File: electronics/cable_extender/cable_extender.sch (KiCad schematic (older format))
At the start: 2 parts

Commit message: added initial connections for the 2.54mm grid (possibly
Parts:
- added J? (x2): Conn_01x08, symbol Connector_Generic:Conn_01x08
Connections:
- net labels added: PIN_01, PIN_02, PIN_03, PIN_04, PIN_05, PIN_06, PIN_07, PIN_08
- wire segments 0 -> 8
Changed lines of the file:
@@
 Wire Notes Line
 	600  7550 1400 7550
+$Comp
+L Connector_Generic:Conn_01x08 J?
+U 1 1 5EE7D502
+P 950 1450
+F 0 "J?" H 868 825 50  0000 C CNN
+F 1 "Conn_01x08" H 868 916 50  0000 C CNN
+F 2 "" H 950 1450 50  0001 C CNN
+F 3 "~" H 950 1450 50  0001 C CNN
+	1    950  1450
+	-1   0    0    1
+$EndComp
+Text Label 1200 1750 0    50   ~ 0
+PIN_01
+Text Label 1200 1650 0    50   ~ 0
+PIN_02
+Text Label 1200 1550 0    50   ~ 0
+PIN_03
+Text Label 1200 1450 0    50   ~ 0
+PIN_04
+Text Label 1200 1350 0    50   ~ 0
+PIN_05
+Text Label 1200 1250 0    50   ~ 0
+PIN_06
+Text Label 1200 1150 0    50   ~ 0
+PIN_07
+Text Label 1200 1050 0    50   ~ 0
+PIN_08
+$Comp
+L Connector_Generic:Conn_01x08 J?
+U 1 1 5EE7E83D
+P 1700 1450
+F 0 "J?" H 1618 825 50  0000 C CNN
+F 1 "Conn_01x08" H 1618 916 50  0000 C CNN
+F 2 "" H 1700 1450 50  0001 C CNN
+F 3 "~" H 1700 1450 50  0001 C CNN
+	1    1700 1450
+	1    0    0    1
+$EndComp
+Wire Wire Line
+	1150 1050 1500 1050
+Wire Wire Line
+	1500 1150 1150 1150
+Wire Wire Line
+	1150 1250 1500 1250
+Wire Wire Line
+	1500 1350 1150 1350
+Wire Wire Line
+	1150 1450 1500 1450
+Wire Wire Line
+	1500 1550 1150 1550
+Wire Wire Line
+	1150 1650 1500 1650
+Wire Wire Line
+	1500 1750 1150 1750
 $EndSCHEMATC

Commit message: updated PCB library, added initial connections
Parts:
- removed J? (x2): Conn_01x08, symbol Connector_Generic:Conn_01x08
- added J? (x2): Conn_01x06, symbol Connector_Generic:Conn_01x06
- added J? (x2): Conn_01x11, symbol Connector_Generic:Conn_01x11
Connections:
- net labels added: PIN_09, PIN_10, PIN_11
- wire segments 8 -> 28
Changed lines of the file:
@@
 Wire Notes Line
 	600  7550 1400 7550
+Text Label 1600 1850 0    50   ~ 0
+PIN_04
+Text Label 1600 1750 0    50   ~ 0
+PIN_05
+Text Label 1600 1650 0    50   ~ 0
+PIN_06
+Text Label 1600 1550 0    50   ~ 0
+PIN_07
+Text Label 1600 1450 0    50   ~ 0
+PIN_08
 $Comp
-L Connector_Generic:Conn_01x08 J?
-U 1 1 5EE7D502
-P 950 1450
-F 0 "J?" H 868 825 50  0000 C CNN
-F 1 "Conn_01x08" H 868 916 50  0000 C CNN
-F 2 "" H 950 1450 50  0001 C CNN
-F 3 "~" H 950 1450 50  0001 C CNN
-	1    950  1450
+L Connector_Generic:Conn_01x06 J?
+U 1 1 5EE7FFB1
+P 1350 1650
+F 0 "J?" H 1350 1250 50  0000 C CNN
+F 1 "Conn_01x06" V 1450 1600 50  0000 C CNN
+F 2 "" H 1350 1650 50  0001 C CNN
+F 3 "~" H 1350 1650 50  0001 C CNN
+	1    1350 1650
 	-1   0    0    1
 $EndComp
-Text Label 1200 1750 0    50   ~ 0
-PIN_01
-Text Label 1200 1650 0    50   ~ 0
-PIN_02
-Text Label 1200 1550 0    50   ~ 0
-PIN_03
-Text Label 1200 1450 0    50   ~ 0
-PIN_04
-Text Label 1200 1350 0    50   ~ 0
-PIN_05
-Text Label 1200 1250 0    50   ~ 0
-PIN_06
-Text Label 1200 1150 0    50   ~ 0
-PIN_07
-Text Label 1200 1050 0    50   ~ 0
-PIN_08
+Wire Wire Line
+	1550 1450 1900 1450
+Wire Wire Line
+	1900 1550 1550 1550
+Wire Wire Line
+	1550 1650 1900 1650
+Wire Wire Line
+	1900 1750 1550 1750
+Wire Wire Line
+	1550 1850 1900 1850
 $Comp
-L Connector_Generic:Conn_01x08 J?
-U 1 1 5EE7E83D
-P 1700 1450
-F 0 "J?" H 1618 825 50  0000 C CNN
-F 1 "Conn_01x08" H 1618 916 50  0000 C CNN
-F 2 "" H 1700 1450 50  0001 C CNN
-F 3 "~" H 1700 1450 50  0001 C CNN
-	1    1700 1450
+L Connector_Generic:Conn_01x06 J?
+U 1 1 5EE82071
+P 2100 1650
+F 0 "J?" H 2100 1250 50  0000 C CNN
+F 1 "Conn_01x06" V 2200 1650 50  0000 C CNN
+F 2 "" H 2100 1650 50  0001 C CNN
+F 3 "~" H 2100 1650 50  0001 C CNN
+	1    2100 1650
 	1    0    0    1
 $EndComp
+Text Label 1600 1350 0    50   ~ 0
+PIN_09
 Wire Wire Line
-	1150 1050 1500 1050
+	1550 1350 1900 1350
+$Comp
+L Connector_Generic:Conn_01x11 J?
+U 1 1 5EE87913
+P 650 1650
+F 0 "J?" H 650 1050 50  0000 C CNN
+F 1 "Conn_01x11" V 750 1650 50  0000 C CNN
+F 2 "" H 650 1650 50  0001 C CNN
+F 3 "~" H 650 1650 50  0001 C CNN
+	1    650  1650
+	-1   0    0    1
+$EndComp
+Text Label 900  2150 0    50   ~ 0
+PIN_01
+Text Label 900  2050 0    50   ~ 0
+PIN_02
+Text Label 900  1950 0    50   ~ 0
+PIN_03
+Text Label 900  1850 0    50   ~ 0
+PIN_04
+Text Label 900  1750 0    50   ~ 0
+PIN_05
+Text Label 900  1650 0    50   ~ 0
+PIN_06
+Text Label 900  1550 0    50   ~ 0
+PIN_07
+Text Label 900  1450 0    50   ~ 0
+PIN_08
+Text Label 900  1350 0    50   ~ 0
+PIN_09
+Text Label 900  1250 0    50   ~ 0
+PIN_10
+Text Label 900  1150 0    50   ~ 0
+PIN_11
 Wire Wire Line
-	1500 1150 1150 1150
+	900  1250 850  1250
 Wire Wire Line
-	1150 1250 1500 1250
+	850  1150 900  1150
 Wire Wire Line
-	1500 1350 1150 1350
+	850  1350 900  1350
 Wire Wire Line
-	1150 1450 1500 1450
+	900  1450 850  1450
 Wire Wire Line
-	1500 1550 1150 1550
+	850  1550 900  1550
 Wire Wire Line
-	1150 1650 1500 1650
+	900  1650 850  1650
 Wire Wire Line
-	1500 1750 1150 1750
+	850  1750 900  1750
+Wire Wire Line
+	900  1850 850  1850
+Wire Wire Line
+	850  1950 900  1950
+Wire Wire Line
+	900  2050 850  2050
+Wire Wire Line
+	850  2150 900  2150
+$Comp
+L Connector_Generic:Conn_01x11 J?
+U 1 1 5EE8F5C8
+P 2800 1650
+F 0 "J?" H 2800 1050 50  0000 C CNN
+F 1 "Conn_01x11" V 2900 1650 50  0000 C CNN
+F 2 "" H 2800 1650 50  0001 C CNN
+F 3 "~" H 2800 1650 50  0001 C CNN
+	1    2800 1650
+	1    0    0    1
+$EndComp
+Text Label 2550 2150 2    50   ~ 0
+PIN_01
+Text Label 2550 2050 2    50   ~ 0
+PIN_02
+Text Label 2550 1950 2    50   ~ 0
+PIN_03
+Text Label 2550 1850 2    50   ~ 0
+PIN_04
+Text Label 2550 1750 2    50   ~ 0
+PIN_05
+Text Label 2550 1650 2    50   ~ 0
+PIN_06
+Text Label 2550 1550 2    50   ~ 0
+PIN_07
+Text Label 2550 1450 2    50   ~ 0
+PIN_08
+Text Label 2550 1350 2    50   ~ 0
+PIN_09
+Text Label 2550 1250 2    50   ~ 0
+PIN_10
+Text Label 2550 1150 2    50   ~ 0
+PIN_11
+Wire Wire Line
+	2550 1250 2600 1250
+Wire Wire Line
+	2600 1150 2550 1150
+Wire Wire Line
+	2600 1350 2550 1350
+Wire Wire Line
+	2550 1450 2600 1450
+Wire Wire Line
+	2600 1550 2550 1550
+Wire Wire Line
+	2550 1650 2600 1650
+Wire Wire Line
+	2600 1750 2550 1750
+Wire Wire Line
+	2550 1850 2600 1850
+Wire Wire Line
+	2600 1950 2550 1950
+Wire Wire Line
+	2550 2050 2600 2050
+Wire Wire Line
+	2600 2150 2550 2150
 $EndSCHEMATC

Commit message: trying out the pitch and matching of the hole grids
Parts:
- J1, J4: renamed from J?; footprint (none) -> SquantorConnectors:hole_row-0254-1X11-H010-ELONG
- J2, J3: renamed from J?; footprint (none) -> SquantorConnectors:hole_row-0508-1X06-H015-ELONG
- N1: value 20200610 -> 20200615
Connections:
- net PIN_01: now also J2.1 (Pin_1), J3.1 (Pin_1)
- net PIN_03: now also J2.2 (Pin_2), J3.2 (Pin_2)
- net PIN_04: no longer J2.1 (Pin_1), J3.1 (Pin_1)
- net PIN_05: now also J2.3 (Pin_3), J3.3 (Pin_3); no longer J2.2 (Pin_2), J3.2 (Pin_2)
- net PIN_06: no longer J2.3 (Pin_3), J3.3 (Pin_3)
- net PIN_08: no longer J2.5 (Pin_5), J3.5 (Pin_5)
- net PIN_09: now also J2.5 (Pin_5), J3.5 (Pin_5); no longer J2.6 (Pin_6), J3.6 (Pin_6)
- net PIN_11: now also J2.6 (Pin_6), J3.6 (Pin_6)
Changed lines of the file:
@@
 P 1050 7450
 F 0 "N1" H 1000 7550 60  0000 L CNN
-F 1 "20200610" H 800 7450 60  0000 L CNN
+F 1 "20200615" H 800 7450 60  0000 L CNN
 F 2 "SquantorLabels:Label_Generic" H 1050 7450 60  0001 C CNN
 F 3 "" H 1050 7450 60  0001 C CNN
@@
 Wire Notes Line
 	600  7550 1400 7550
-Text Label 1600 1850 0    50   ~ 0
-PIN_04
-Text Label 1600 1750 0    50   ~ 0
-PIN_05
-Text Label 1600 1650 0    50   ~ 0
-PIN_06
-Text Label 1600 1550 0    50   ~ 0
-PIN_07
-Text Label 1600 1450 0    50   ~ 0
-PIN_08
 $Comp
-L Connector_Generic:Conn_01x06 J?
+L Connector_Generic:Conn_01x06 J2
 U 1 1 5EE7FFB1
 P 1350 1650
-F 0 "J?" H 1350 1250 50  0000 C CNN
+F 0 "J2" H 1350 1250 50  0000 C CNN
 F 1 "Conn_01x06" V 1450 1600 50  0000 C CNN
-F 2 "" H 1350 1650 50  0001 C CNN
+F 2 "SquantorConnectors:hole_row-0508-1X06-H015-ELONG" H 1350 1650 50  0001 C CNN
 F 3 "~" H 1350 1650 50  0001 C CNN
 	1    1350 1650
@@
 	1550 1850 1900 1850
 $Comp
-L Connector_Generic:Conn_01x06 J?
+L Connector_Generic:Conn_01x06 J3
 U 1 1 5EE82071
 P 2100 1650
-F 0 "J?" H 2100 1250 50  0000 C CNN
+F 0 "J3" H 2100 1250 50  0000 C CNN
 F 1 "Conn_01x06" V 2200 1650 50  0000 C CNN
-F 2 "" H 2100 1650 50  0001 C CNN
+F 2 "SquantorConnectors:hole_row-0508-1X06-H015-ELONG" H 2100 1650 50  0001 C CNN
 F 3 "~" H 2100 1650 50  0001 C CNN
 	1    2100 1650
 	1    0    0    1
 $EndComp
-Text Label 1600 1350 0    50   ~ 0
-PIN_09
 Wire Wire Line
 	1550 1350 1900 1350
 $Comp
-L Connector_Generic:Conn_01x11 J?
+L Connector_Generic:Conn_01x11 J1
 U 1 1 5EE87913
 P 650 1650
-F 0 "J?" H 650 1050 50  0000 C CNN
+F 0 "J1" H 650 1050 50  0000 C CNN
 F 1 "Conn_01x11" V 750 1650 50  0000 C CNN
-F 2 "" H 650 1650 50  0001 C CNN
+F 2 "SquantorConnectors:hole_row-0254-1X11-H010-ELONG" H 650 1650 50  0001 C CNN
 F 3 "~" H 650 1650 50  0001 C CNN
 	1    650  1650
@@
 	850  2150 900  2150
 $Comp
-L Connector_Generic:Conn_01x11 J?
+L Connector_Generic:Conn_01x11 J4
 U 1 1 5EE8F5C8
 P 2800 1650
-F 0 "J?" H 2800 1050 50  0000 C CNN
+F 0 "J4" H 2800 1050 50  0000 C CNN
 F 1 "Conn_01x11" V 2900 1650 50  0000 C CNN
-F 2 "" H 2800 1650 50  0001 C CNN
+F 2 "SquantorConnectors:hole_row-0254-1X11-H010-ELONG" H 2800 1650 50  0001 C CNN
 F 3 "~" H 2800 1650 50  0001 C CNN
 	1    2800 1650
@@
 Wire Wire Line
 	2600 2150 2550 2150
+Text Label 1600 1850 0    50   ~ 0
+PIN_01
+Text Label 1600 1750 0    50   ~ 0
+PIN_03
+Text Label 1600 1650 0    50   ~ 0
+PIN_05
+Text Label 1600 1550 0    50   ~ 0
+PIN_07
+Text Label 1600 1450 0    50   ~ 0
+PIN_09
+Text Label 1600 1350 0    50   ~ 0
+PIN_11
 $EndSCHEMATC

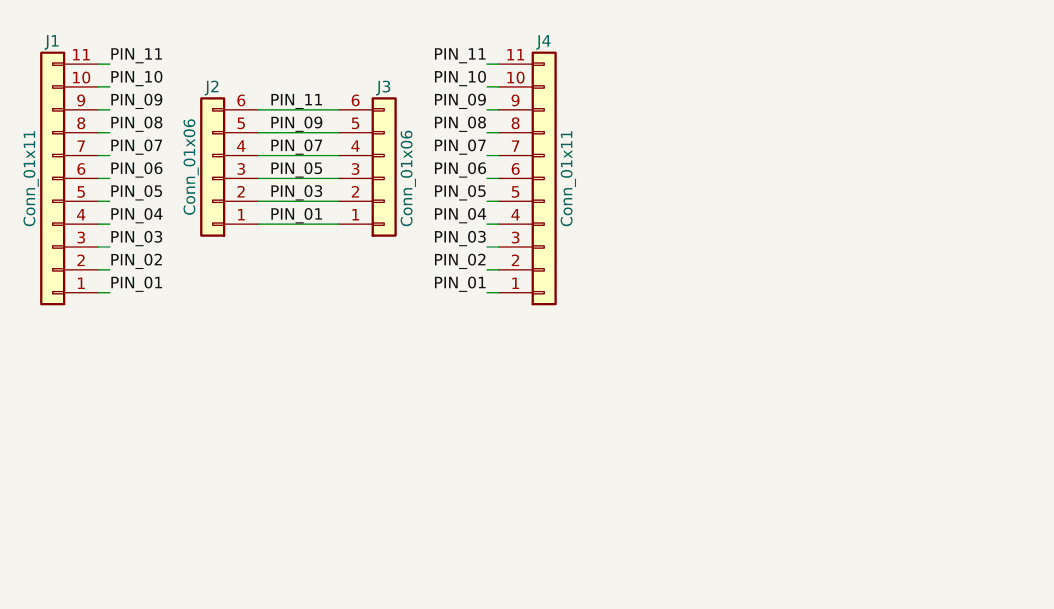
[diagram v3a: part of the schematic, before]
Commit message: added more hole rows
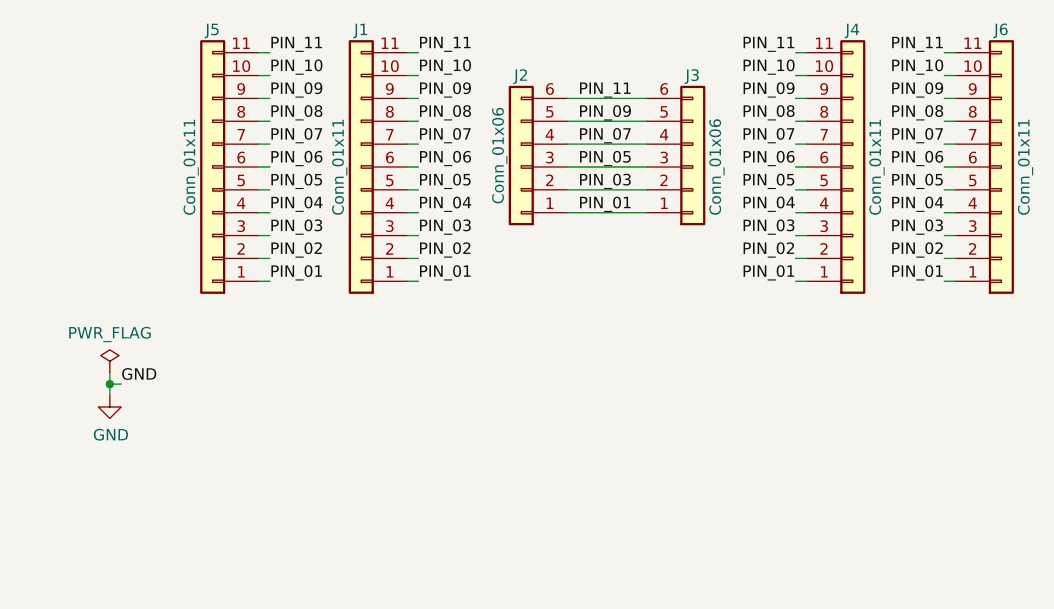
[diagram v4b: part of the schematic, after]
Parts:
- added J5, J6: Conn_01x11, SquantorConnectors:hole_row-0250-1X11-H010-ELONG, symbol Connector_Generic:Conn_01x11
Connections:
- net PIN_01: now also J5.1 (Pin_1), J6.1 (Pin_1)
- net PIN_02: now also J5.2 (Pin_2), J6.2 (Pin_2)
- net PIN_03: now also J5.3 (Pin_3), J6.3 (Pin_3)
- net PIN_04: now also J5.4 (Pin_4), J6.4 (Pin_4)
- net PIN_05: now also J5.5 (Pin_5), J6.5 (Pin_5)
- net PIN_06: now also J5.6 (Pin_6), J6.6 (Pin_6)
- net PIN_07: now also J5.7 (Pin_7), J6.7 (Pin_7)
- net PIN_08: now also J5.8 (Pin_8), J6.8 (Pin_8)
- net PIN_09: now also J5.9 (Pin_9), J6.9 (Pin_9)
- net PIN_10: now also J5.10 (Pin_10), J6.10 (Pin_10)
- net PIN_11: now also J5.11 (Pin_11), J6.11 (Pin_11)
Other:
- moved on the sheet: J1, J2, J3, J4

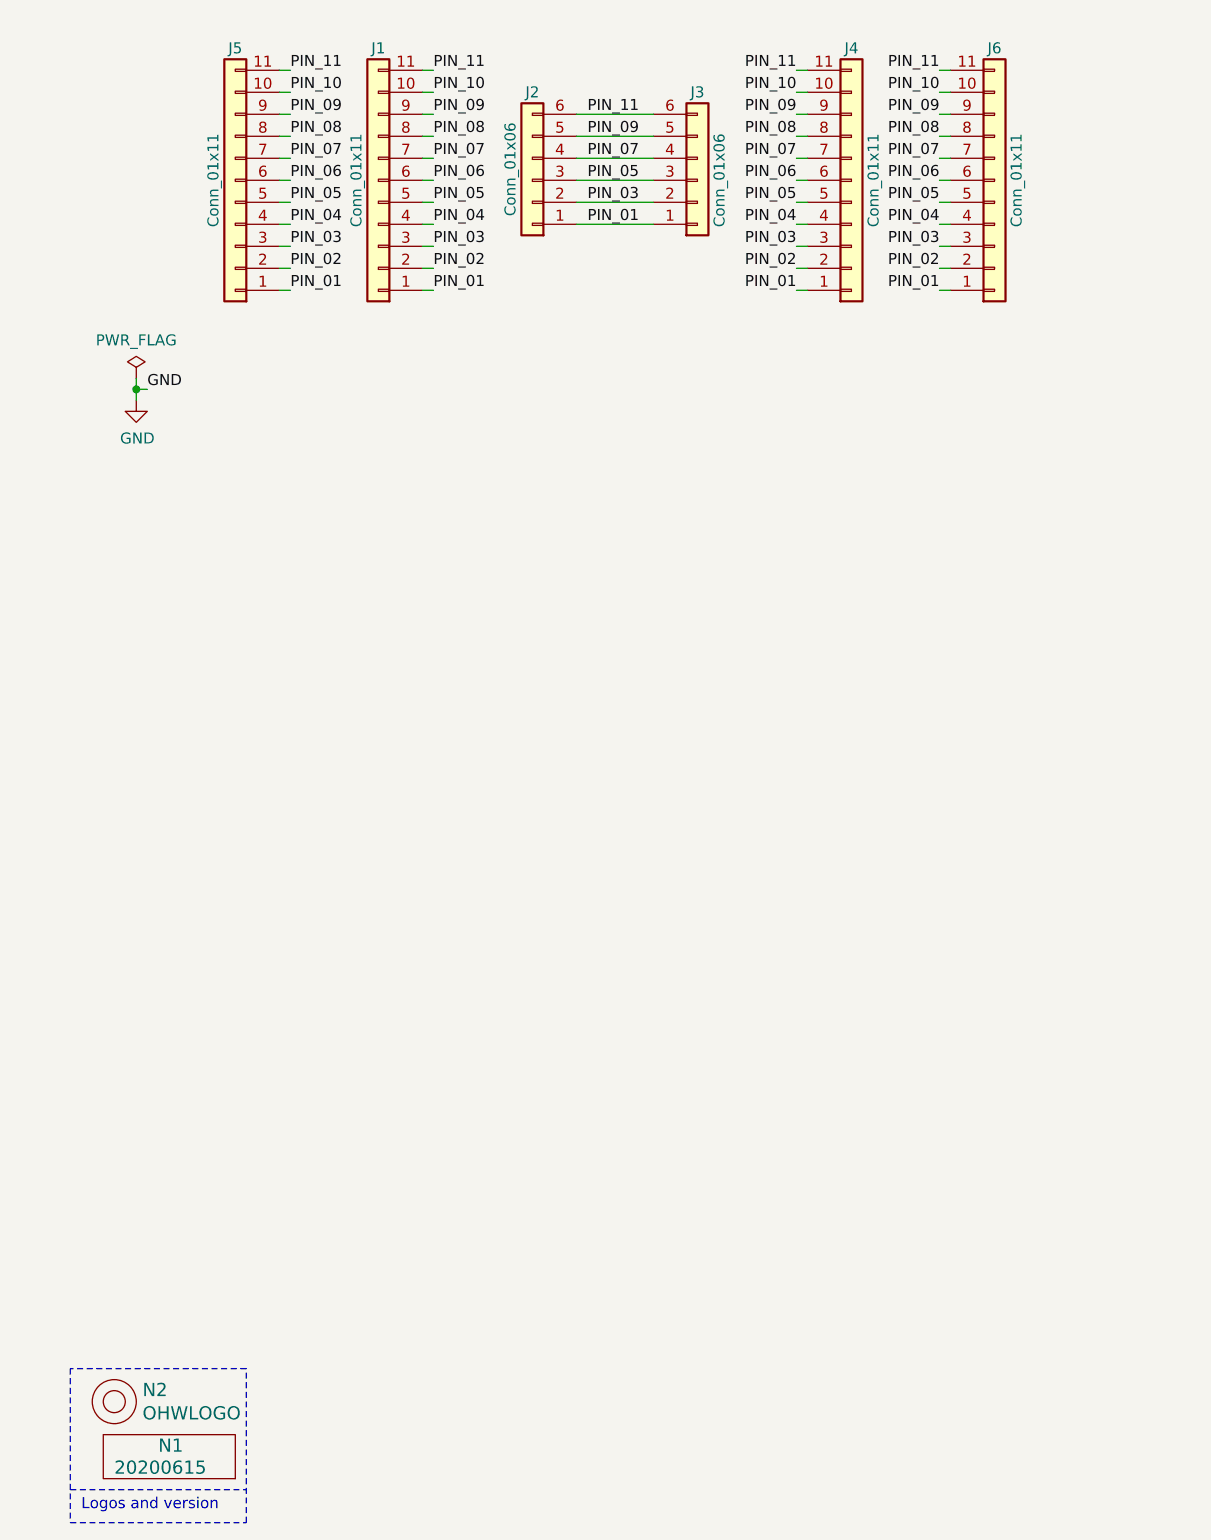
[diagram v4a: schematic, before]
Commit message: rearranged connector positions
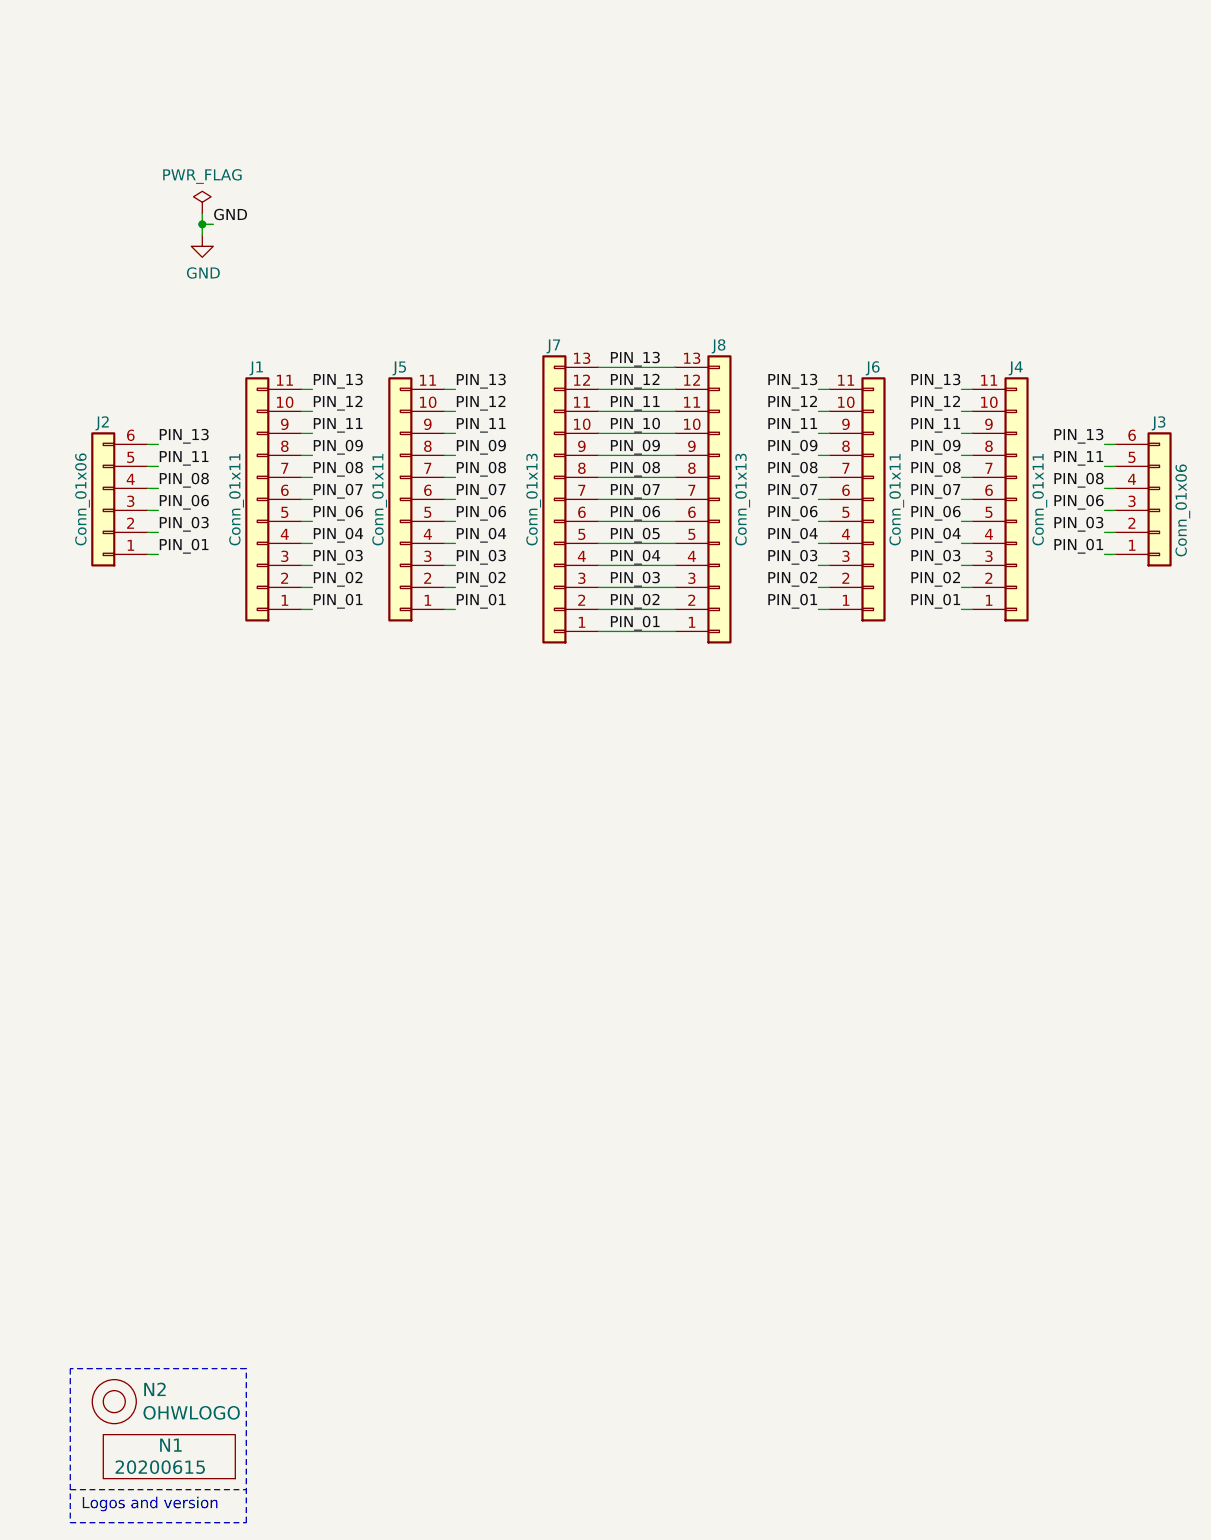
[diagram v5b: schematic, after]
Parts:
- added J7, J8: Conn_01x13, SquantorConnectors:hole_row-0200-1X13-H008-ELONG, symbol Connector_Generic:Conn_01x13
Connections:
- net PIN_01: now also J7.1 (Pin_1), J8.1 (Pin_1)
- net PIN_02: now also J7.2 (Pin_2), J8.2 (Pin_2)
- net PIN_03: now also J7.3 (Pin_3), J8.3 (Pin_3)
- net PIN_04: now also J7.4 (Pin_4), J8.4 (Pin_4)
- net PIN_05: now also J7.5 (Pin_5), J8.5 (Pin_5); no longer J1.5 (Pin_5), J2.3 (Pin_3), J3.3 (Pin_3), J4.5 (Pin_5), J5.5 (Pin_5), J6.5 (Pin_5)
- net PIN_06: now also J1.5 (Pin_5), J2.3 (Pin_3), J3.3 (Pin_3), J4.5 (Pin_5), J5.5 (Pin_5), J6.5 (Pin_5), J7.6 (Pin_6), J8.6 (Pin_6); no longer J1.6 (Pin_6), J4.6 (Pin_6), J5.6 (Pin_6), J6.6 (Pin_6)
- net PIN_07: now also J1.6 (Pin_6), J4.6 (Pin_6), J5.6 (Pin_6), J6.6 (Pin_6), J7.7 (Pin_7), J8.7 (Pin_7); no longer J1.7 (Pin_7), J2.4 (Pin_4), J3.4 (Pin_4), J4.7 (Pin_7), J5.7 (Pin_7), J6.7 (Pin_7)
- net PIN_08: now also J1.7 (Pin_7), J2.4 (Pin_4), J3.4 (Pin_4), J4.7 (Pin_7), J5.7 (Pin_7), J6.7 (Pin_7), J7.8 (Pin_8), J8.8 (Pin_8); no longer J1.8 (Pin_8), J4.8 (Pin_8), J5.8 (Pin_8), J6.8 (Pin_8)
- net PIN_09: now also J1.8 (Pin_8), J4.8 (Pin_8), J5.8 (Pin_8), J6.8 (Pin_8), J7.9 (Pin_9), J8.9 (Pin_9); no longer J1.9 (Pin_9), J2.5 (Pin_5), J3.5 (Pin_5), J4.9 (Pin_9), J5.9 (Pin_9), J6.9 (Pin_9)
- net PIN_10: now also J7.10 (Pin_10), J8.10 (Pin_10); no longer J1.10 (Pin_10), J4.10 (Pin_10), J5.10 (Pin_10), J6.10 (Pin_10)
- net PIN_11: now also J1.9 (Pin_9), J2.5 (Pin_5), J3.5 (Pin_5), J4.9 (Pin_9), J5.9 (Pin_9), J6.9 (Pin_9), J7.11 (Pin_11), J8.11 (Pin_11); no longer J1.11 (Pin_11), J2.6 (Pin_6), J3.6 (Pin_6), J4.11 (Pin_11), J5.11 (Pin_11), J6.11 (Pin_11)
- new net PIN_12: J1.10 (Pin_10), J4.10 (Pin_10), J5.10 (Pin_10), J6.10 (Pin_10), J7.12 (Pin_12), J8.12 (Pin_12)
- new net PIN_13: J1.11 (Pin_11), J2.6 (Pin_6), J3.6 (Pin_6), J4.11 (Pin_11), J5.11 (Pin_11), J6.11 (Pin_11), J7.13 (Pin_13), J8.13 (Pin_13)
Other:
- moved on the sheet: J1, J2, J3, J4, J5, J6
